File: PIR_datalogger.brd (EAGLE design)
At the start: 47.8 x 31.7 mm, 21 parts, among them J3 FTDI, J4 ISP, Q2 NPN, U1 ATMEGA328P-MU, U8 MCP1703/3.3V, Y1 16MHZ

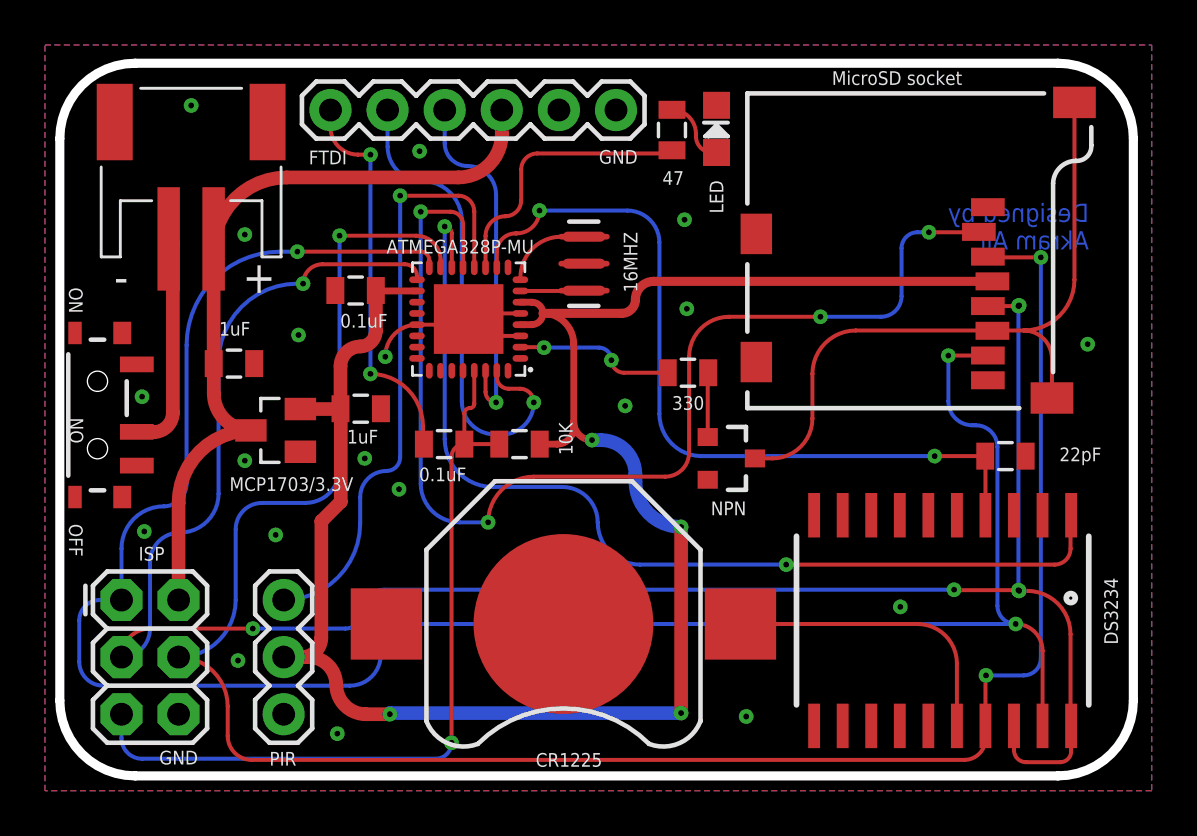
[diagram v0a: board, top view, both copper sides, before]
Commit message: v0.2 - design changes
* Removed NPN transistor - microSD cards use their own sleep mode -
keeping up with new SD protocol
* Added decoupling cap to microSD card
* Added pullups to microSD card and RTC
* Adjusted some traces
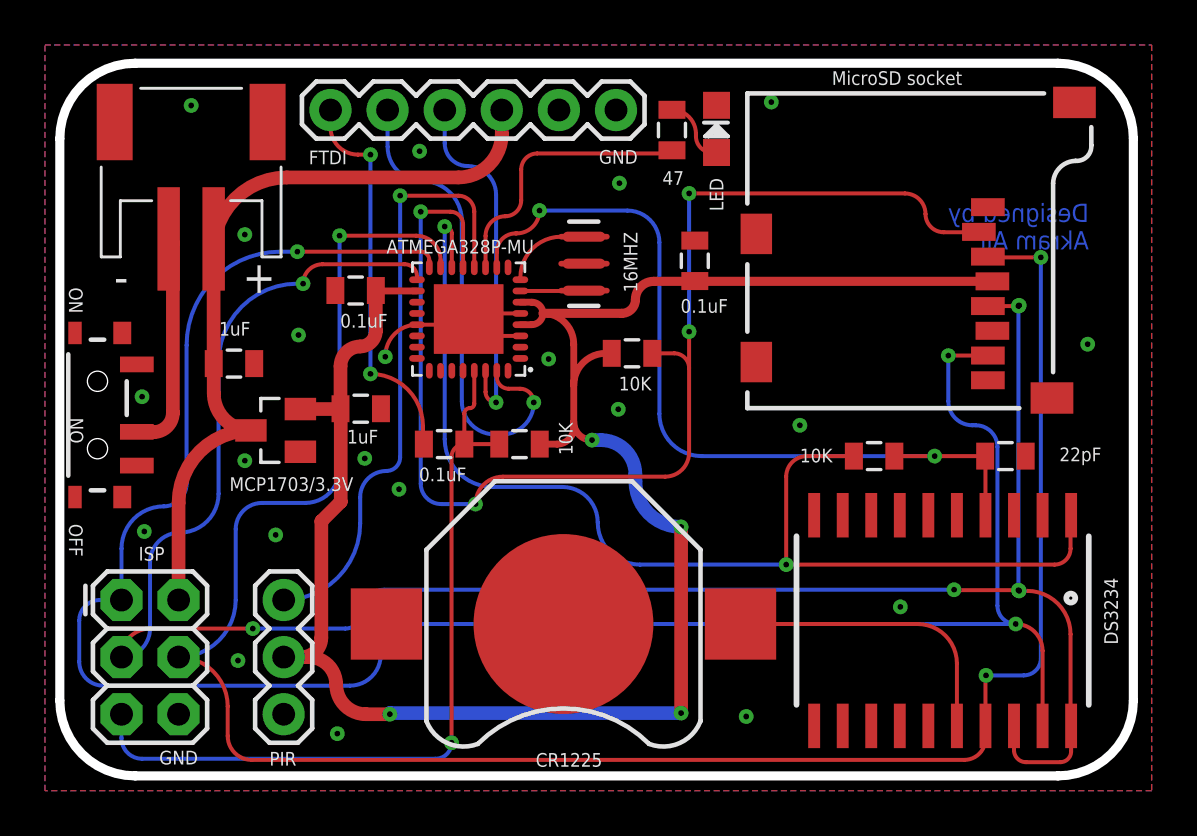
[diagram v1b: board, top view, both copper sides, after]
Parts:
- removed Q2: NPN, SparkFun-DiscreteSemi:SOT23-3
- added C3: 0.1uF, SparkFun-Passives:0805
- added R1: 10K, SparkFun-Passives:0805
- R2: value 330 -> 10K
- moved R2 9.07 mm to (46.9, 37.0)
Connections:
- removed net GND0: JP1.GND, JP1.GND1, JP1.GND3, Q2.3
- removed net N$6: Q2.1, R2.2
- net D4: no longer R2.1
- net D6: now also R2.2
- net D9: now also R1.1
- net GND: now also C3.2, JP1.GND, JP1.GND1, JP1.GND3; no longer Q2.2
- net SS: now also R2.1
- net VCC: now also C3.1, R1.2
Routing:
- net GND0: track 30.1 -> 0.00 mm
- net SS: track 43.4 -> 50.7 mm
- net D4: track 7.02 -> 0.00 mm, vias 2 -> 0
- net D9: track 50.8 -> 56.5 mm
- net N$6: track 2.87 -> 0.00 mm
- net VCC: track 86.5 -> 88.8 mm
- net D6: track 34.8 -> 36.6 mm
- net GND: vias 19 -> 21
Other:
- board text added: "v0.2 | February 2017"
- board text removed: "v0.1 | January 2017"
